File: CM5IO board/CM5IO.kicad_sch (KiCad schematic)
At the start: 47 parts, among them J1 RBUS, J11 USB_C_Receptacle_USB2.0, U1 ESP32-S3, Y1 R940000171

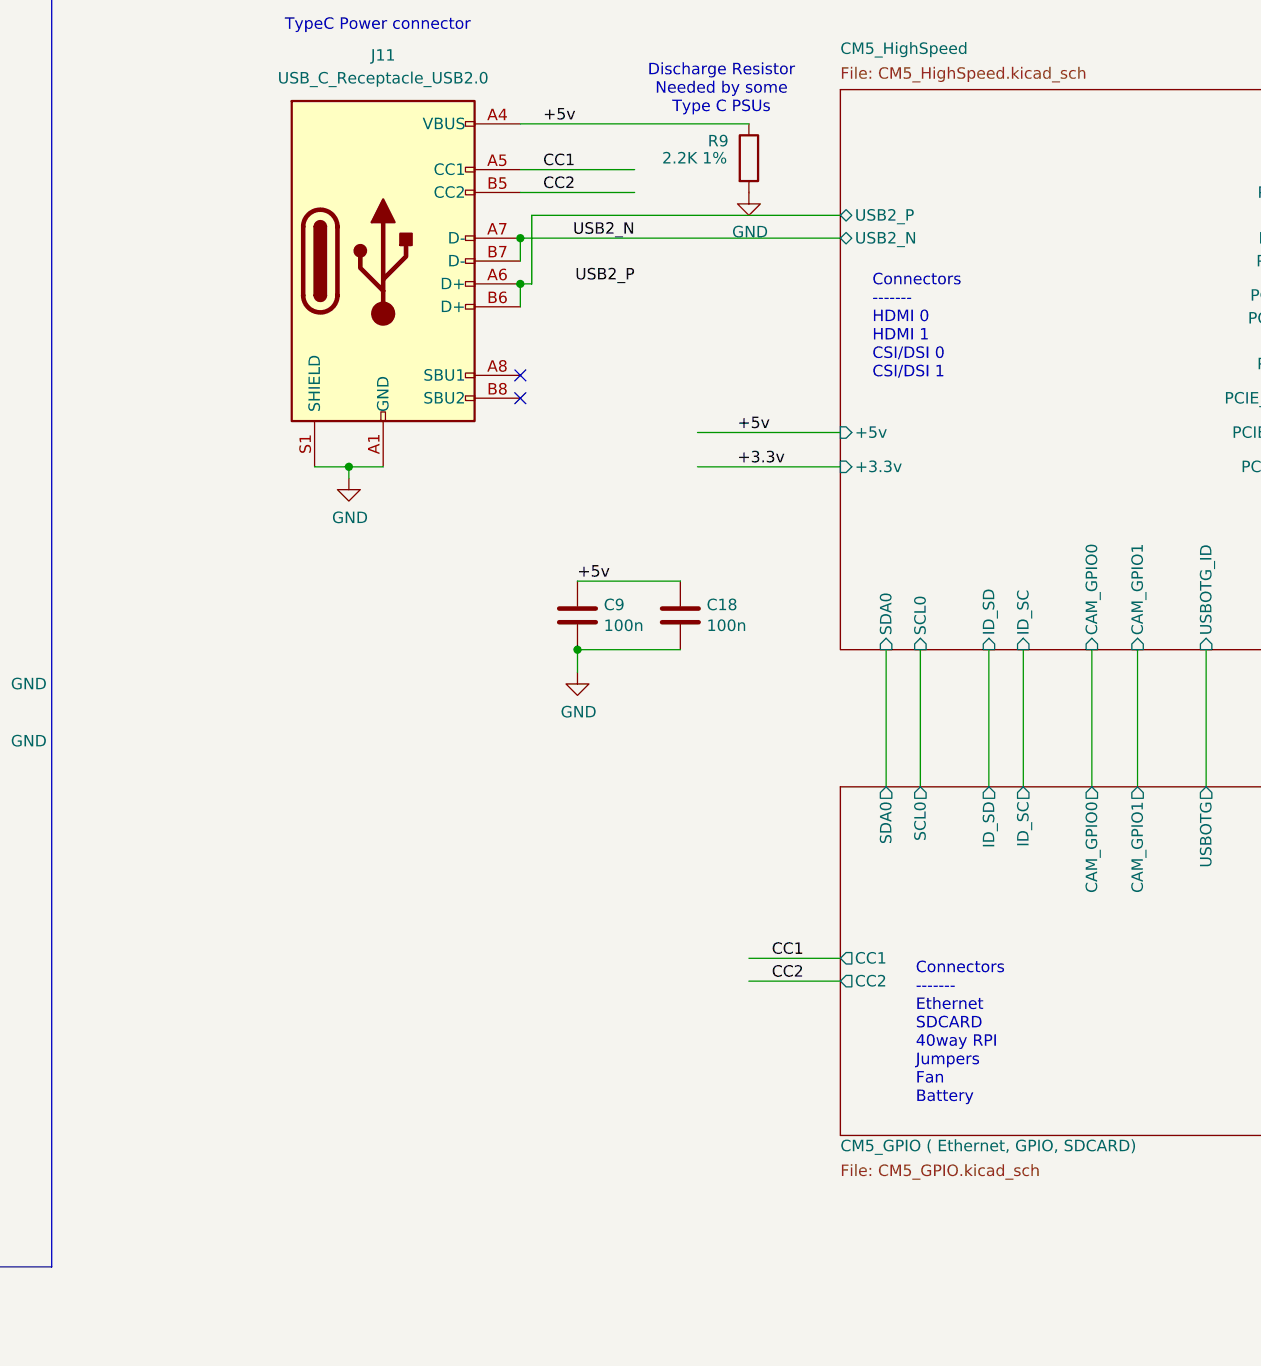
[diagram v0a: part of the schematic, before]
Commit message: Duplicated additional USB-C in sch.
How to change pin label on CM5?
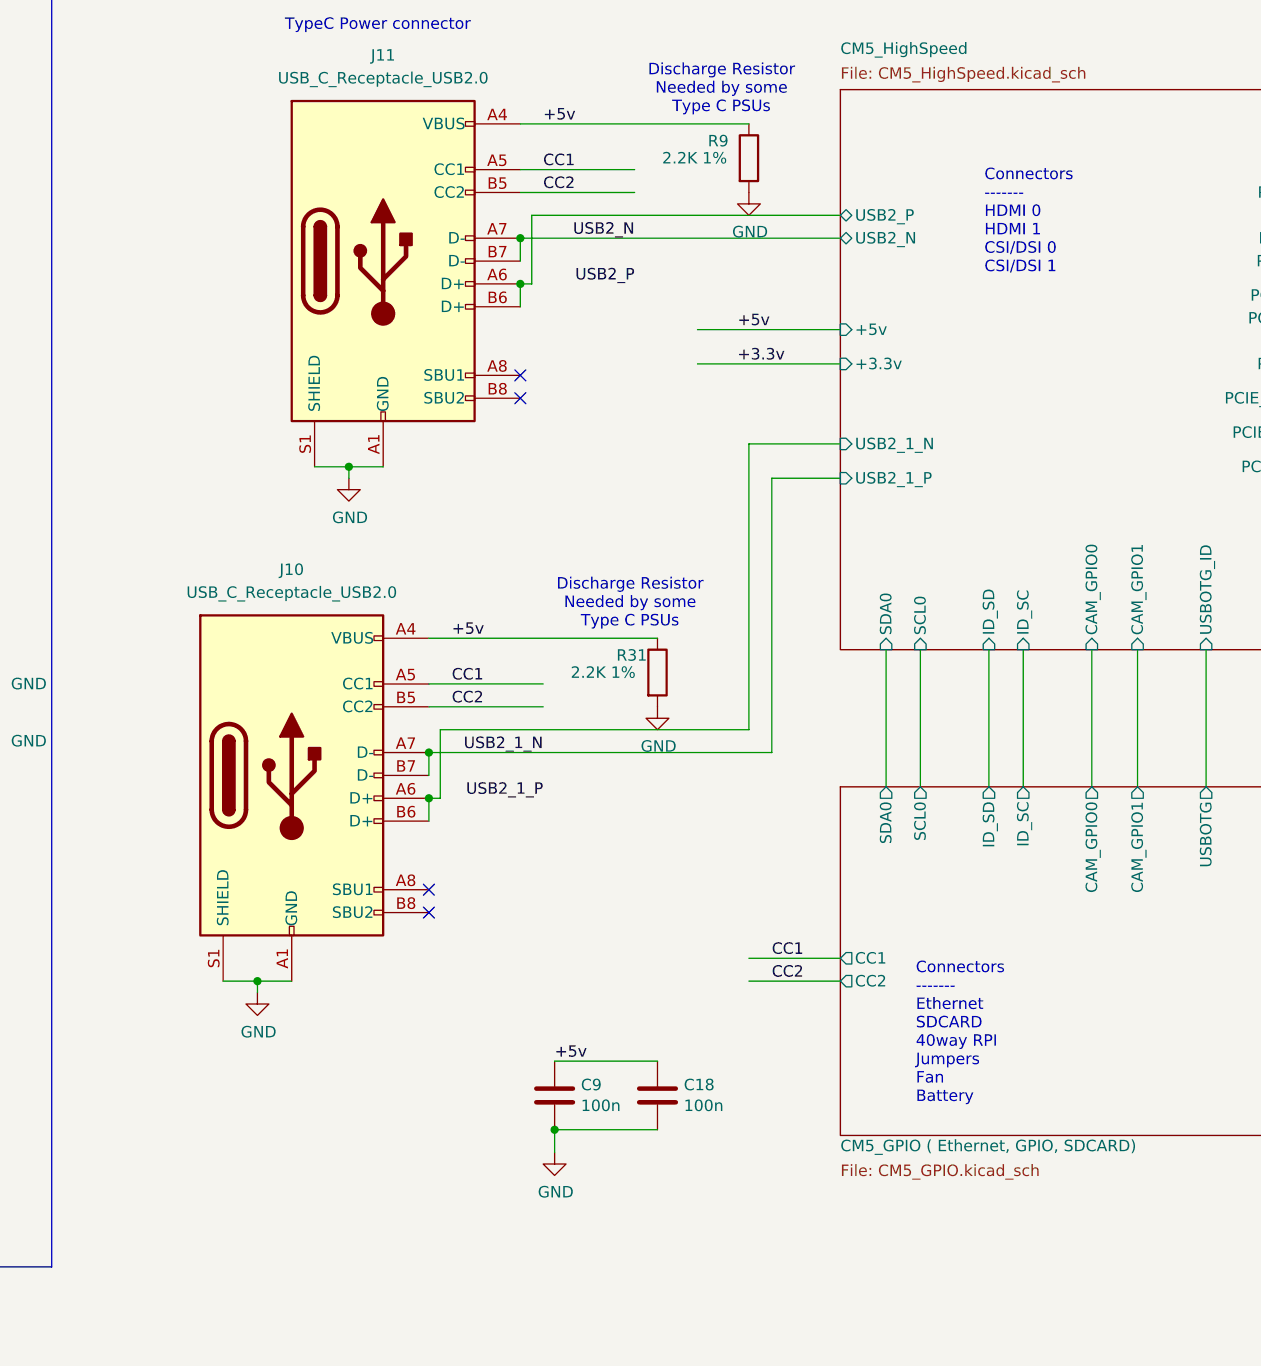
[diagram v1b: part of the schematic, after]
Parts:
- added J10: USB_C_Receptacle_USB2.0, Connector_USB:USB_C_Receptacle_GCT_USB4105-xx-A_16P_TopMnt_Horizontal, symbol Connector:USB_C_Receptacle_USB2.0_16P
- added R31: 2.2K 1%, Resistor_SMD:R_0402_1005Metric, symbol Device:R
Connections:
- net +5v: now also J10.A4 (VBUS), J10.A9 (VBUS), J10.B4 (VBUS), J10.B9 (VBUS), R31.1
- net CC1: now also J10.A5 (CC1)
- net CC2: now also J10.B5 (CC2)
- net GND: now also J10.A1 (GND), J10.A12 (GND), J10.B1 (GND), J10.B12 (GND), J10.S1 (SHIELD), R31.2
- new net CM5_HighSpeed/USB2_1_N: J10.A6 (D+), J10.B6 (D+)
- new net USB2_1_N: J10.A7 (D-), J10.B7 (D-)
- no-connect marks 13 -> 15
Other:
- sheet CM5_HighSpeed ports: added USB2_1_N, USB2_1_P; removed none
- moved on the sheet: C18, C9

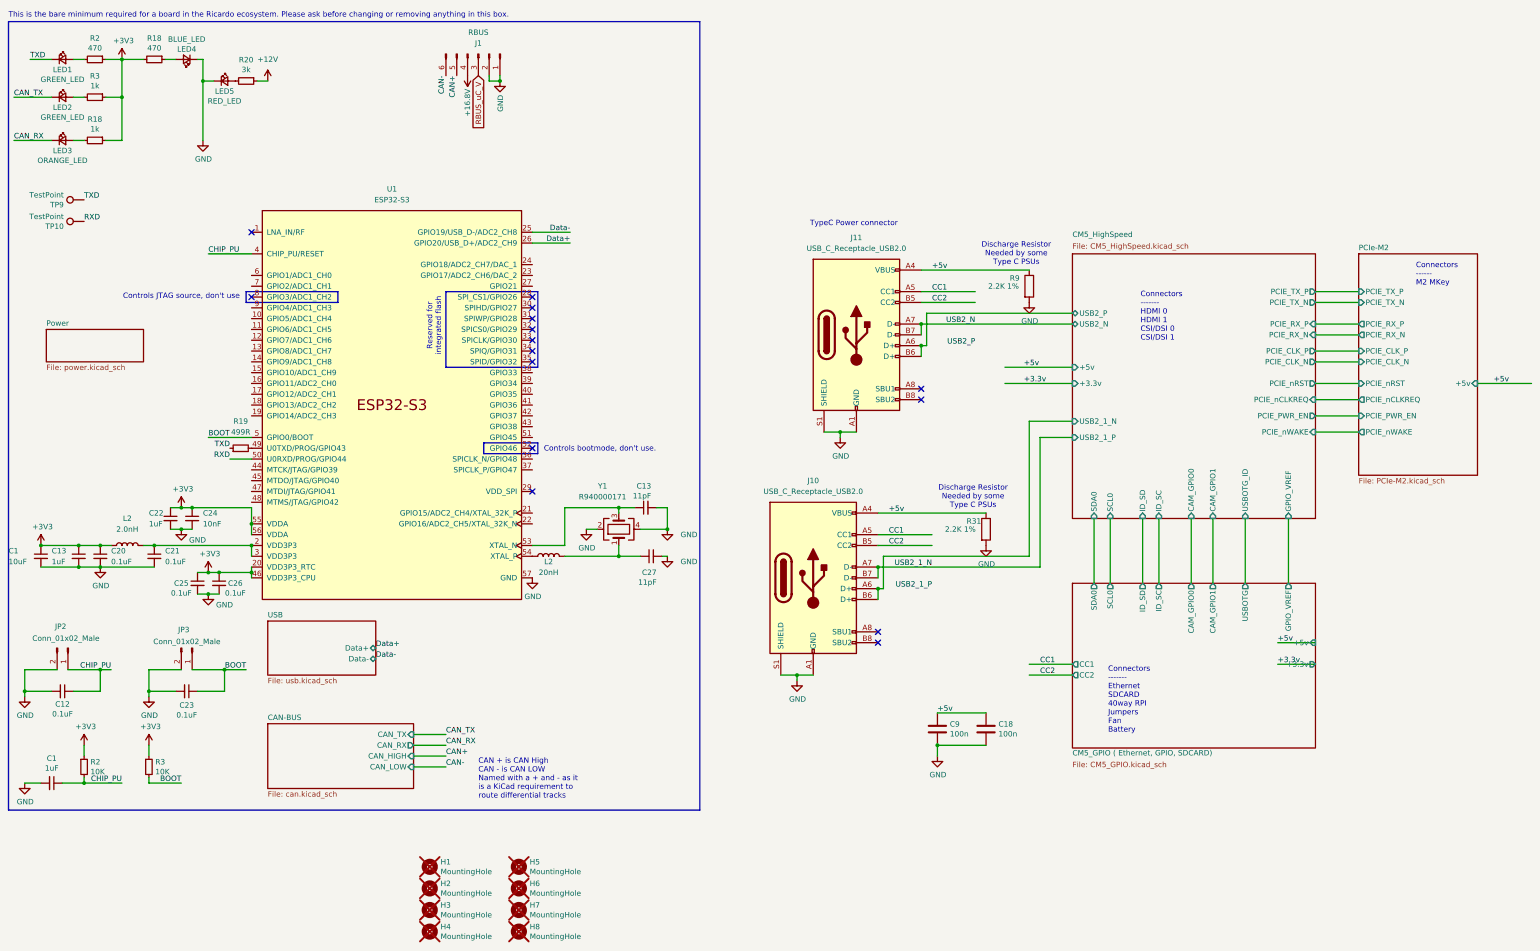
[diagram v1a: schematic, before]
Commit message: Moved Ricardo to hierarchical sheet in main sch.
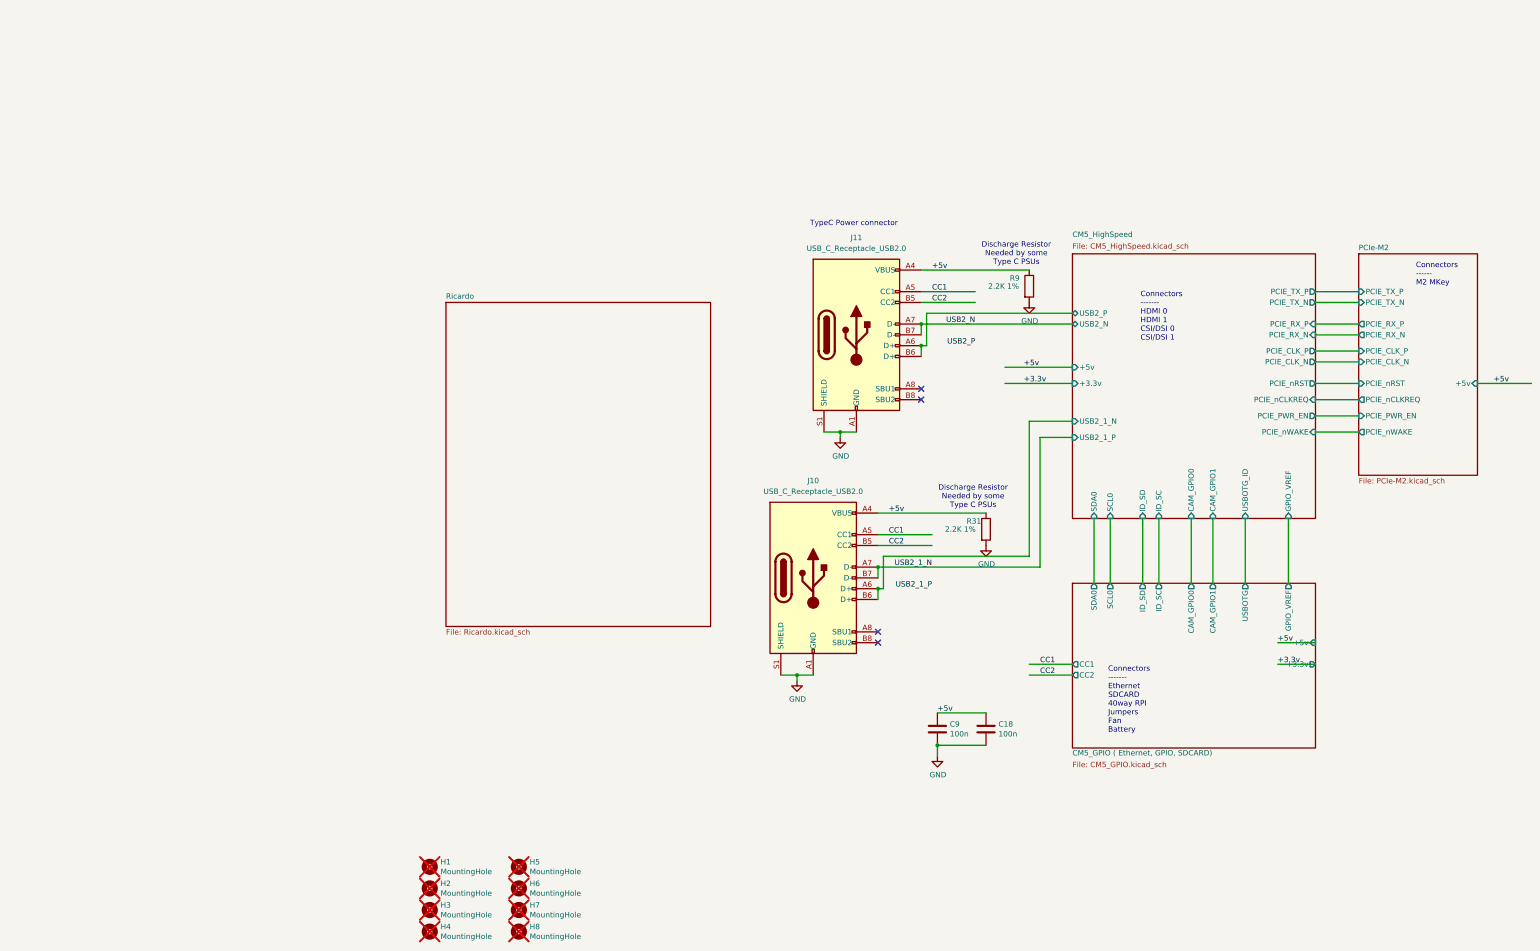
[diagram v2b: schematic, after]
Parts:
- removed C1, C13, C22: 1uF, Capacitor_SMD:C_0402_1005Metric, symbol Device:C_Small
- removed C1: 10uF, Capacitor_SMD:C_0402_1005Metric, symbol Device:C_Small
- removed C12, C20, C21, C23, C25, C26: 0.1uF, Capacitor_SMD:C_0402_1005Metric, symbol Device:C_Small
- removed C13, C27: 11pF, Capacitor_SMD:C_0402_1005Metric, symbol Device:C_Small
- removed C24: 10nF, Capacitor_SMD:C_0402_1005Metric, symbol Device:C_Small
- removed J1: RBUS, iclr:Molex_Mini-Fit_Jr_5569-06A2_2x03_P4.20mm_Horizontal, symbol Connector:Conn_01x06_Male
- removed JP2, JP3: Conn_01x02_Male, Connector_PinHeader_2.54mm:PinHeader_1x02_P2.54mm_Vertical, symbol Connector:Conn_01x02_Male
- removed L2: 2.0nH, Inductor_SMD:L_0402_1005Metric, symbol Device:L
- removed L2: 20nH, Inductor_SMD:L_0402_1005Metric, symbol Device:L
- removed LED1, LED2: GREEN_LED, LED_SMD:LED_0402_1005Metric, symbol Device:LED_Small
- removed LED3: ORANGE_LED, LED_SMD:LED_0402_1005Metric, symbol Device:LED_Small
- removed LED4: BLUE_LED, LED_SMD:LED_0402_1005Metric, symbol Device:LED_Small
- removed LED5: RED_LED, LED_SMD:LED_0402_1005Metric, symbol Device:LED_Small
- removed R18, R3: 1k, Resistor_SMD:R_0402_1005Metric, symbol Device:R_Small
- removed R18, R2: 470, Resistor_SMD:R_0402_1005Metric, symbol Device:R_Small
- removed R19: 499R, Resistor_SMD:R_0402_1005Metric, symbol Device:R_Small
- removed R2, R3: 10K, Resistor_SMD:R_0402_1005Metric, symbol Device:R_Small
- removed R20: 3k, Resistor_SMD:R_0402_1005Metric, symbol Device:R_Small
- removed TP10, TP9: TestPoint, TestPoint:TestPoint_Pad_D1.0mm, symbol Connector:TestPoint
- removed U1: ESP32-S3, iclr:QFN40P700X700X90-57N, symbol Espressif:ESP32-S3
- removed Y1: R940000171, iclr:Crystal_SMD_2016-4Pin_2.0x1.6mm, symbol Device:Crystal_GND24
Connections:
- no-connect marks 15 -> 4
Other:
- removed sheet CAN-BUS
- removed sheet Power
- removed sheet USB
- added sheet Ricardo (Ricardo.kicad_sch)
- note removed: "CAN + is CAN High CAN - is CAN LOW Named with a + and - as it is a KiCad requirement to route differential tracks"
- note removed: "Controls JTAG source, don't use"
- note removed: "Controls bootmode, don't use."
- note removed: "Reserved for integrated flash"
- note removed: "This is the bare minimum required for a board in the Ricardo ecosystem. Please ask before changing or removing anything in this box."
